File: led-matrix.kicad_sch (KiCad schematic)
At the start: 67 parts, among them U1 MAX7219, U1 Pico

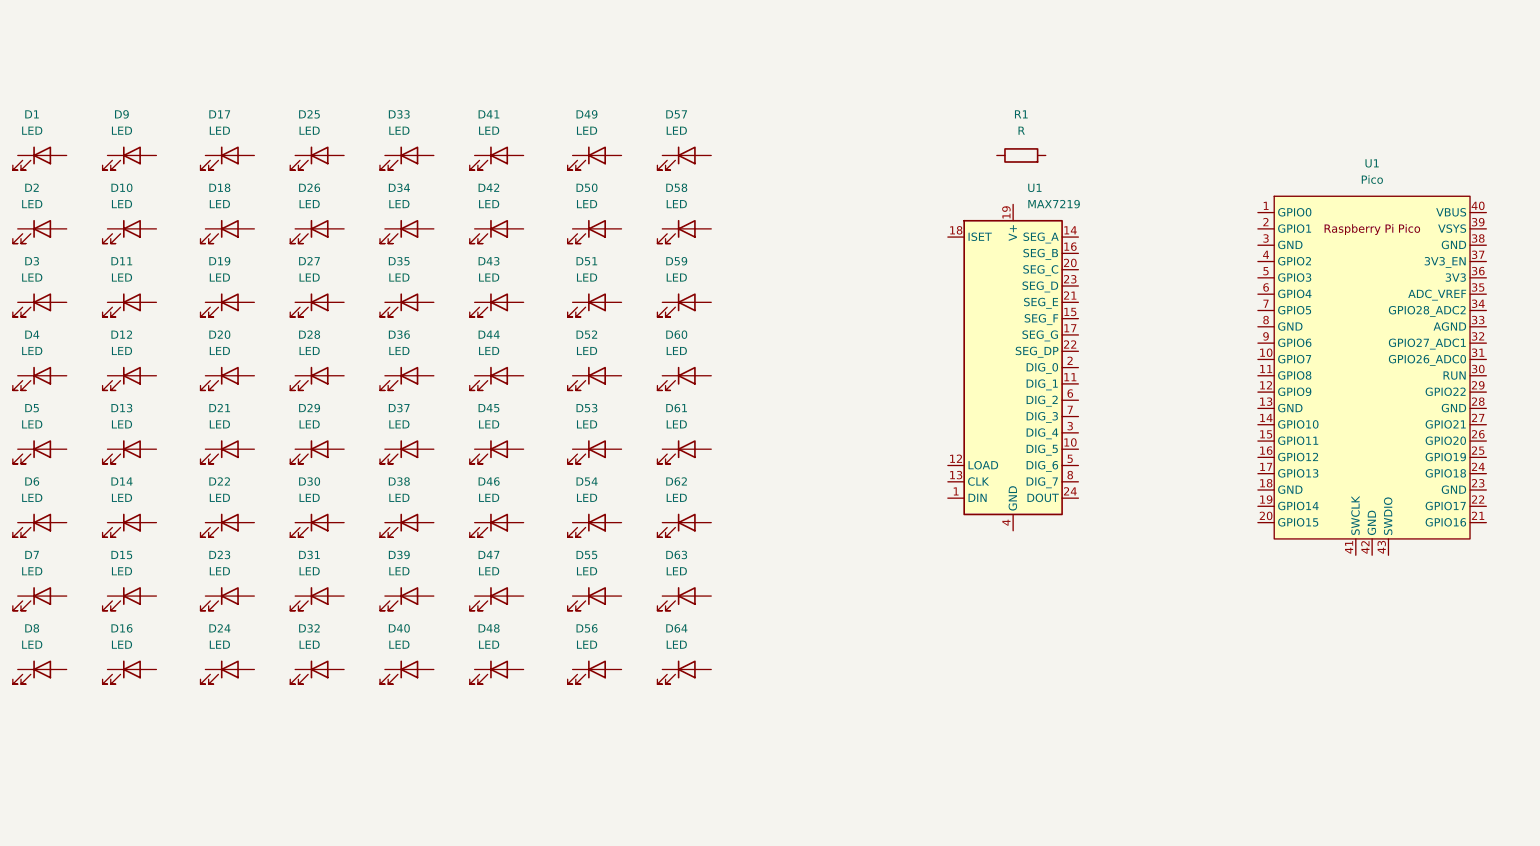
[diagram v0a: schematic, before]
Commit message: feat: add grounding cap
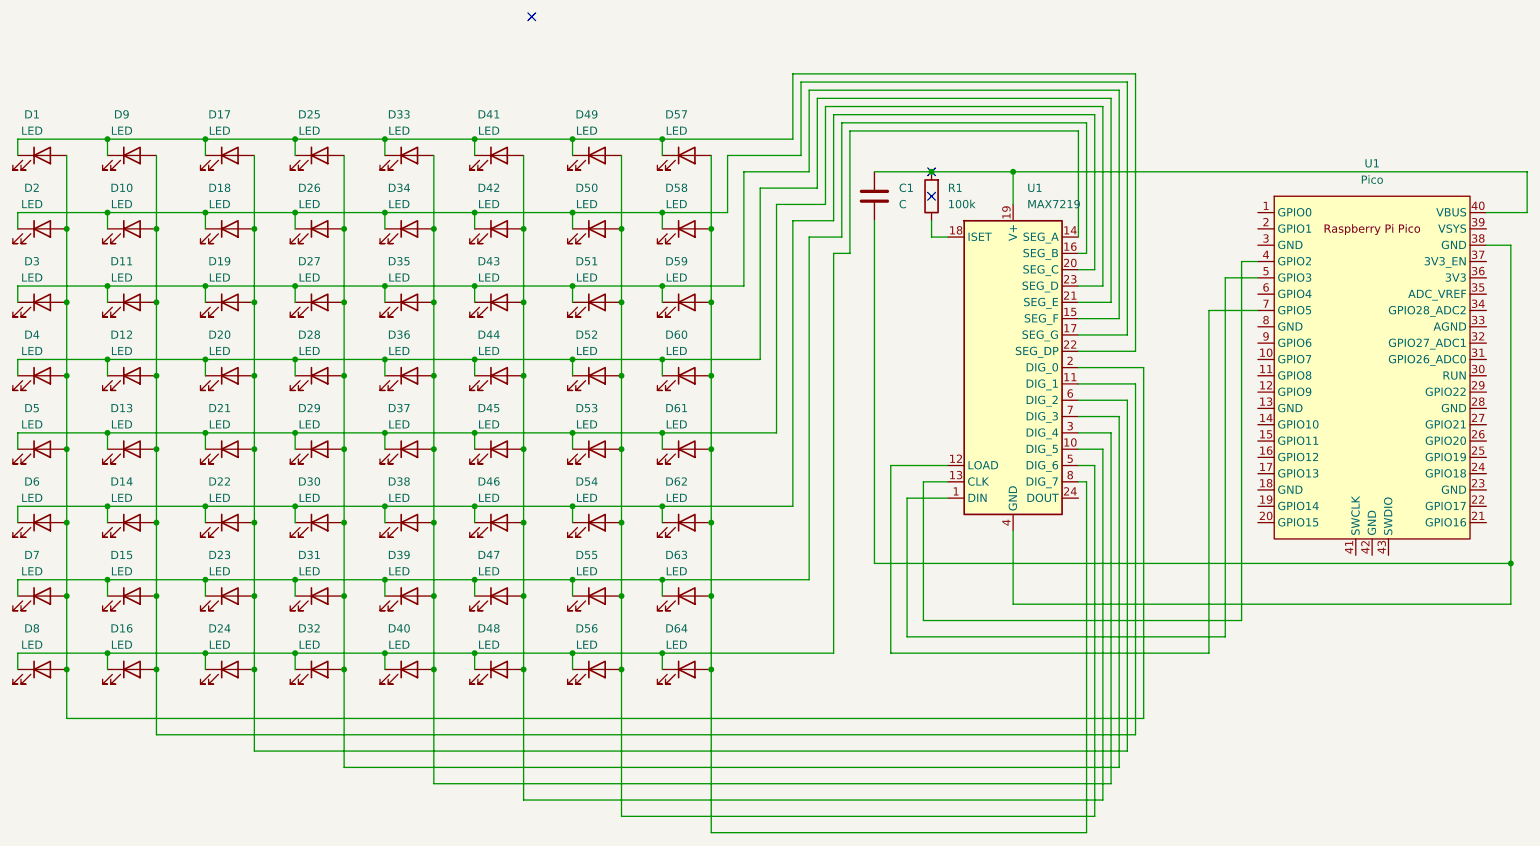
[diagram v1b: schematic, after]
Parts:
- added C1: C, symbol Device:C
- R1: value R -> 100k
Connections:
- net at D51.1 (K): now also D11.1 (K), D19.1 (K), D27.1 (K), D3.1 (K), D35.1 (K), D43.1 (K), D59.1 (K), U1.15 (SEG_F)
- net at D51.2 (A): now also D49.2 (A), D50.2 (A), D52.2 (A), D53.2 (A), D54.2 (A), D55.2 (A), D56.2 (A), U1.5 (DIG_6)
- net at D59.2 (A): now also D57.2 (A), D58.2 (A), D60.2 (A), D61.2 (A), D62.2 (A), D63.2 (A), D64.2 (A), U1.8 (DIG_7)
- net at D58.1 (K): now also D10.1 (K), D18.1 (K), D2.1 (K), D26.1 (K), D34.1 (K), D42.1 (K), D50.1 (K), U1.17 (SEG_G)
- net at D2.2 (A): now also D1.2 (A), D3.2 (A), D4.2 (A), D5.2 (A), D6.2 (A), D7.2 (A), D8.2 (A), U1.2 (DIG_0)
- net at D42.2 (A): now also D41.2 (A), D43.2 (A), D44.2 (A), D45.2 (A), D46.2 (A), D47.2 (A), D48.2 (A), U1.10 (DIG_5)
- net at D14.1 (K): now also D22.1 (K), D30.1 (K), D38.1 (K), D46.1 (K), D54.1 (K), D6.1 (K), D62.1 (K), U1.20 (SEG_C)
- net at D14.2 (A): now also D10.2 (A), D11.2 (A), D12.2 (A), D13.2 (A), D15.2 (A), D16.2 (A), D9.2 (A), U1.11 (DIG_1)
- net at D30.2 (A): now also D25.2 (A), D26.2 (A), D27.2 (A), D28.2 (A), D29.2 (A), D31.2 (A), D32.2 (A), U1.7 (DIG_3)
- net at D38.2 (A): now also D33.2 (A), D34.2 (A), D35.2 (A), D36.2 (A), D37.2 (A), D39.2 (A), D40.2 (A), U1.3 (DIG_4)
- net at D17.1 (K): now also D1.1 (K), D25.1 (K), D33.1 (K), D41.1 (K), D49.1 (K), D57.1 (K), D9.1 (K), U1.22 (SEG_DP)
- net at D17.2 (A): now also D18.2 (A), D19.2 (A), D20.2 (A), D21.2 (A), D22.2 (A), D23.2 (A), D24.2 (A), U1.6 (DIG_2)
- net at D28.1 (K): now also D12.1 (K), D20.1 (K), D36.1 (K), D4.1 (K), D44.1 (K), D52.1 (K), D60.1 (K), U1.21 (SEG_E)
- net at D64.1 (K): now also D16.1 (K), D24.1 (K), D32.1 (K), D40.1 (K), D48.1 (K), D56.1 (K), D8.1 (K), U1.14 (SEG_A)
- net at D61.1 (K): now also D13.1 (K), D21.1 (K), D29.1 (K), D37.1 (K), D45.1 (K), D5.1 (K), D53.1 (K), U1.23 (SEG_D)
- net at D15.1 (K): now also D23.1 (K), D31.1 (K), D39.1 (K), D47.1 (K), D55.1 (K), D63.1 (K), D7.1 (K), U1.16 (SEG_B)
- net at U1.1 (DIN): now also U1.5 (GPIO3)
- net at U1.12 (LOAD): now also U1.7 (GPIO5)
- net at U1.13 (CLK): now also U1.4 (GPIO2)
- net at U1.18 (ISET): now also R1.1
- net at U1.19 (V+): now also R1.2, U1.40 (VBUS), C1.1
- net at U1.4 (GND), U1.9 (GND): now also U1.38 (GND), C1.2
- no-connect marks 0 -> 3
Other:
- moved on the sheet: R1

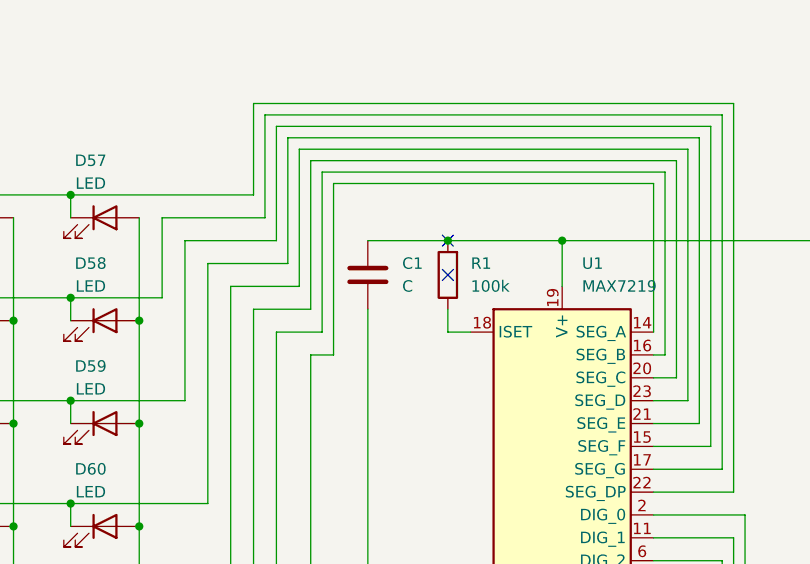
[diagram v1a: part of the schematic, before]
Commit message: chore: set cap size to 100n
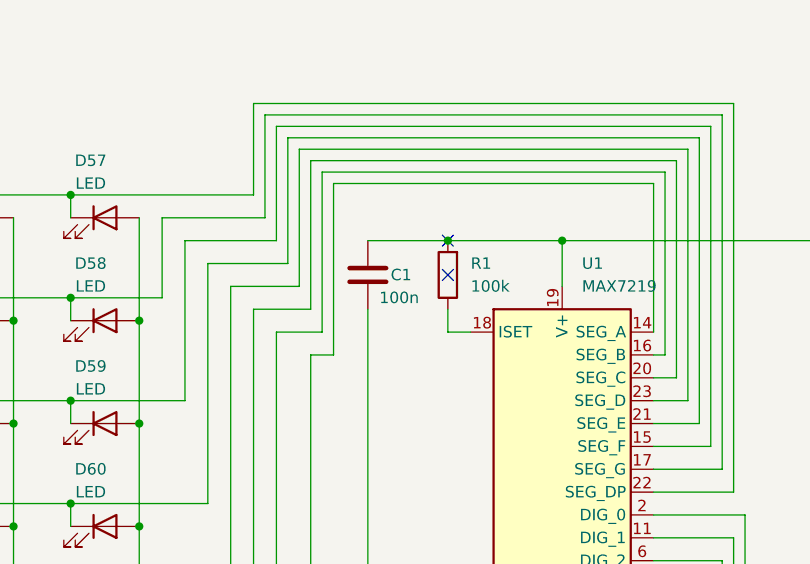
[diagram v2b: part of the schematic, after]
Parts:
- C1: value C -> 100n
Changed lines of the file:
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@@
 		(on_board yes)
 		(dnp no)
-		(fields_autoplaced yes)
 		(property "Reference" "C1"
-			(at 162.56 41.9099 0)
+			(at 161.29 43.18 0)
 			(effects
 				(font
@@
 			)
 		)
-		(property "Value" "C"
-			(at 162.56 44.4499 0)
+		(property "Value" "100n"
+			(at 160.02 45.72 0)
 			(effects
 				(font

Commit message: feat: add touchpads
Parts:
- added J1: Touch Pad x4, symbol Connector:Conn_01x04_Pin
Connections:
- net at U1.10 (GPIO7): now also J1.2 (Pin_2)
- net at U1.11 (GPIO8): now also J1.3 (Pin_3)
- net at U1.12 (GPIO9): now also J1.4 (Pin_4)
- net at U1.9 (GPIO6): now also J1.1 (Pin_1)
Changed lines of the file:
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@@
 	(wire
 		(pts
-			(xy 213.36 55.88) (xy 213.36 111.76)
+			(xy 215.9 55.88) (xy 215.9 113.03)
 		)
 		(stroke
@@
 	(wire
 		(pts
-			(xy 218.44 53.34) (xy 215.9 53.34)
+			(xy 218.44 53.34) (xy 217.17 53.34)
 		)
 		(stroke
@@
 	(wire
 		(pts
+			(xy 212.09 33.02) (xy 212.09 66.04)
+		)
+		(stroke
+			(width 0)
+			(type default)
+		)
+	)
+	(wire
+		(pts
+			(xy 218.44 33.02) (xy 212.09 33.02)
+		)
+		(stroke
+			(width 0)
+			(type default)
+		)
+	)
+	(wire
+		(pts
 			(xy 82.55 102.87) (xy 82.55 105.41)
 		)
@@
 	(wire
 		(pts
-			(xy 218.44 60.96) (xy 210.82 60.96)
+			(xy 218.44 60.96) (xy 214.63 60.96)
 		)
 		(stroke
@@
 	(wire
 		(pts
-			(xy 210.82 60.96) (xy 210.82 114.3)
+			(xy 214.63 60.96) (xy 214.63 114.3)
 		)
 		(stroke
@@
 	(wire
 		(pts
+			(xy 210.82 30.48) (xy 210.82 68.58)
+		)
+		(stroke
+			(width 0)
+			(type default)
+		)
+	)
+	(wire
+		(pts
 			(xy 170.18 49.53) (xy 167.64 49.53)
 		)
@@
 	(wire
 		(pts
-			(xy 210.82 114.3) (xy 161.29 114.3)
+			(xy 214.63 114.3) (xy 161.29 114.3)
 		)
 		(stroke
@@
 	(wire
 		(pts
+			(xy 209.55 71.12) (xy 218.44 71.12)
+		)
+		(stroke
+			(width 0)
+			(type default)
+		)
+	)
+	(wire
+		(pts
 			(xy 133.35 59.69) (xy 133.35 71.12)
 		)
@@
 	(wire
 		(pts
-			(xy 257.81 106.68) (xy 257.81 100.33)
+			(xy 257.81 101.6) (xy 257.81 100.33)
 		)
 		(stroke
@@
 	(wire
 		(pts
-			(xy 166.37 109.22) (xy 166.37 87.63)
+			(xy 166.37 111.76) (xy 166.37 87.63)
 		)
 		(stroke
@@
 	(wire
 		(pts
+			(xy 218.44 30.48) (xy 210.82 30.48)
+		)
+		(stroke
+			(width 0)
+			(type default)
+		)
+	)
+	(wire
+		(pts
 			(xy 190.5 67.31) (xy 199.39 67.31)
 		)
@@
 	(wire
 		(pts
+			(xy 218.44 25.4) (xy 208.28 25.4)
+		)
+		(stroke
+			(width 0)
+			(type default)
+		)
+	)
+	(wire
+		(pts
 			(xy 25.4 116.84) (xy 25.4 114.3)
 		)
@@
 	(wire
 		(pts
+			(xy 208.28 25.4) (xy 208.28 73.66)
+		)
+		(stroke
+			(width 0)
+			(type default)
+		)
+	)
+	(wire
+		(pts
 			(xy 161.29 114.3) (xy 161.29 85.09)
 		)
@@
 	(wire
 		(pts
+			(xy 210.82 68.58) (xy 218.44 68.58)
+		)
+		(stroke
+			(width 0)
+			(type default)
+		)
+	)
+	(wire
+		(pts
 			(xy 96.52 91.44) (xy 111.76 91.44)
 		)
@@
 	(wire
 		(pts
-			(xy 213.36 111.76) (xy 163.83 111.76)
+			(xy 215.9 113.03) (xy 163.83 113.03)
 		)
 		(stroke
@@
 	(wire
 		(pts
-			(xy 218.44 55.88) (xy 213.36 55.88)
+			(xy 218.44 55.88) (xy 215.9 55.88)
 		)
 		(stroke
@@
 	(wire
 		(pts
-			(xy 215.9 53.34) (xy 215.9 109.22)
+			(xy 217.17 53.34) (xy 217.17 111.76)
 		)
 		(stroke
@@
 	(wire
 		(pts
+			(xy 218.44 27.94) (xy 209.55 27.94)
+		)
+		(stroke
+			(width 0)
+			(type default)
+		)
+	)
+	(wire
+		(pts
 			(xy 76.2 93.98) (xy 76.2 105.41)
 		)
@@
 	(wire
 		(pts
-			(xy 180.34 95.25) (xy 180.34 106.68)
+			(xy 180.34 95.25) (xy 180.34 101.6)
 		)
 		(stroke
@@
 	(wire
 		(pts
-			(xy 163.83 111.76) (xy 163.83 90.17)
+			(xy 212.09 66.04) (xy 218.44 66.04)
+		)
+		(stroke
+			(width 0)
+			(type default)
+		)
+	)
+	(wire
+		(pts
+			(xy 209.55 27.94) (xy 209.55 71.12)
+		)
+		(stroke
+			(width 0)
+			(type default)
+		)
+	)
+	(wire
+		(pts
+			(xy 163.83 113.03) (xy 163.83 90.17)
 		)
 		(stroke
@@
 	(wire
 		(pts
-			(xy 215.9 109.22) (xy 166.37 109.22)
+			(xy 217.17 111.76) (xy 166.37 111.76)
 		)
 		(stroke
@@
 	(wire
 		(pts
-			(xy 180.34 106.68) (xy 257.81 106.68)
+			(xy 180.34 101.6) (xy 257.81 101.6)
 		)
 		(stroke
@@
 	(wire
 		(pts
+			(xy 208.28 73.66) (xy 218.44 73.66)
+		)
+		(stroke
+			(width 0)
+			(type default)
+		)
+	)
+	(wire
+		(pts
 			(xy 76.2 71.12) (xy 76.2 82.55)
 		)
@@
 					(unit 1)
 				)
+			)
+		)
+	)
+	(symbol
+		(lib_id "Connector:Conn_01x04_Pin")
+		(at 223.52 30.48 180)
+		(unit 1)
+		(exclude_from_sim no)
+		(in_bom yes)
+		(on_board yes)
+		(dnp no)
+		(fields_autoplaced yes)
+		(property "Reference" "J1"
+			(at 224.79 27.9399 0)
+			(effects
+				(font
+					(size 1.27 1.27)
+				)
+				(justify right)
+			)
+		)
+		(property "Value" "Touch Pad x4"
+			(at 224.79 30.4799 0)
+			(effects
+				(font
+					(size 1.27 1.27)
+				)
+				(justify right)
+			)
+		)
+		(property "Footprint" ""
+			(at 223.52 30.48 0)
+			(effects
+				(font
+					(size 1.27 1.27)
+				)
+				(hide yes)
+			)
+		)
+		(property "Datasheet" "~"
+			(at 223.52 30.48 0)
+			(effects
+				(font
+					(size 1.27 1.27)
+				)
+				(hide yes)
+			)
+		)
+		(property "Description" "Generic connector, single row, 01x04, script generated"
+			(at 223.52 30.48 0)
+			(effects
+				(font
+					(size 1.27 1.27)
+				)
+				(hide yes)
+			)
+		)
+		(pin "1"
+		)
+		(pin "2"
+		)
+		(pin "3"
+		)
+		(pin "4"
+		)
+		(instances
+			(project ""
+				(path "/14dbb19e-a51b-4674-aa79-c96e0324fb3f"
+					(reference "J1")
+					(unit 1)
+				)
